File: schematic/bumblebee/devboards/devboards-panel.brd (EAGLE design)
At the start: 60 x 52 mm, 8 parts

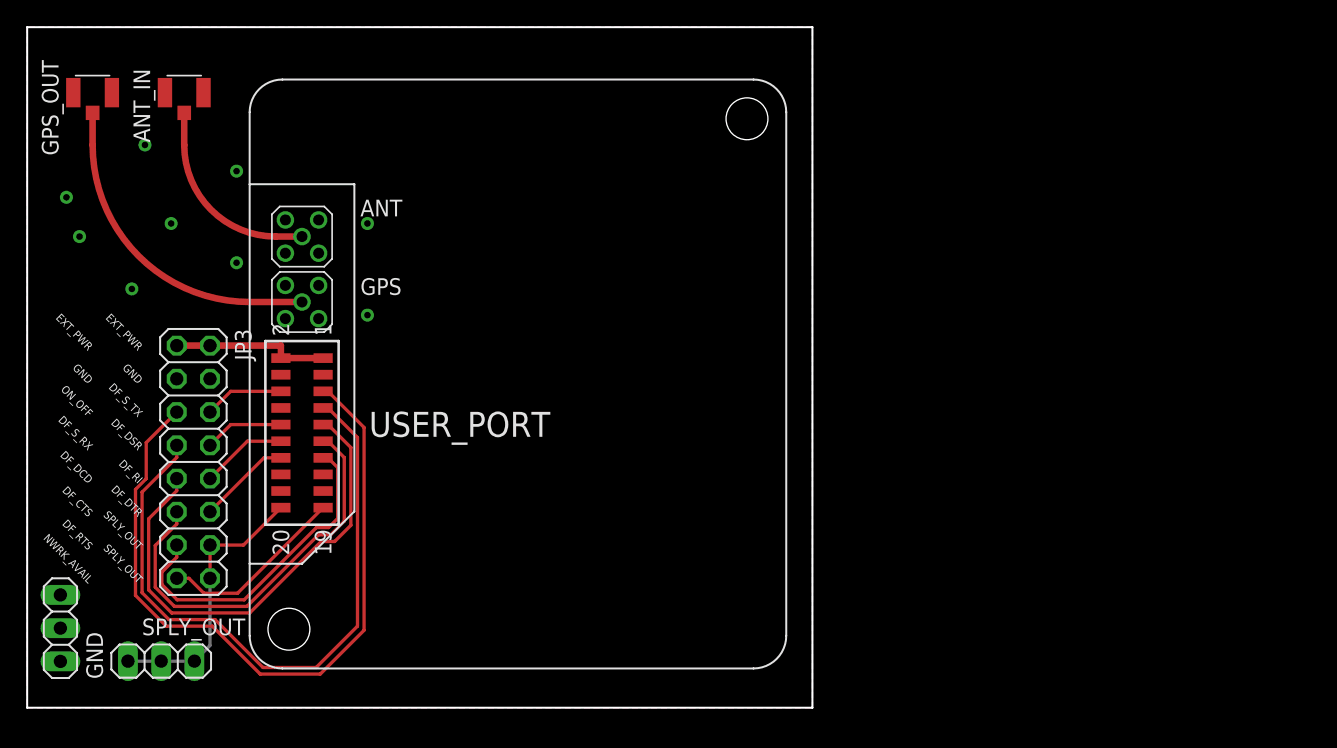
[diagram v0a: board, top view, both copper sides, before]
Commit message: собираем все платы в один шаблон
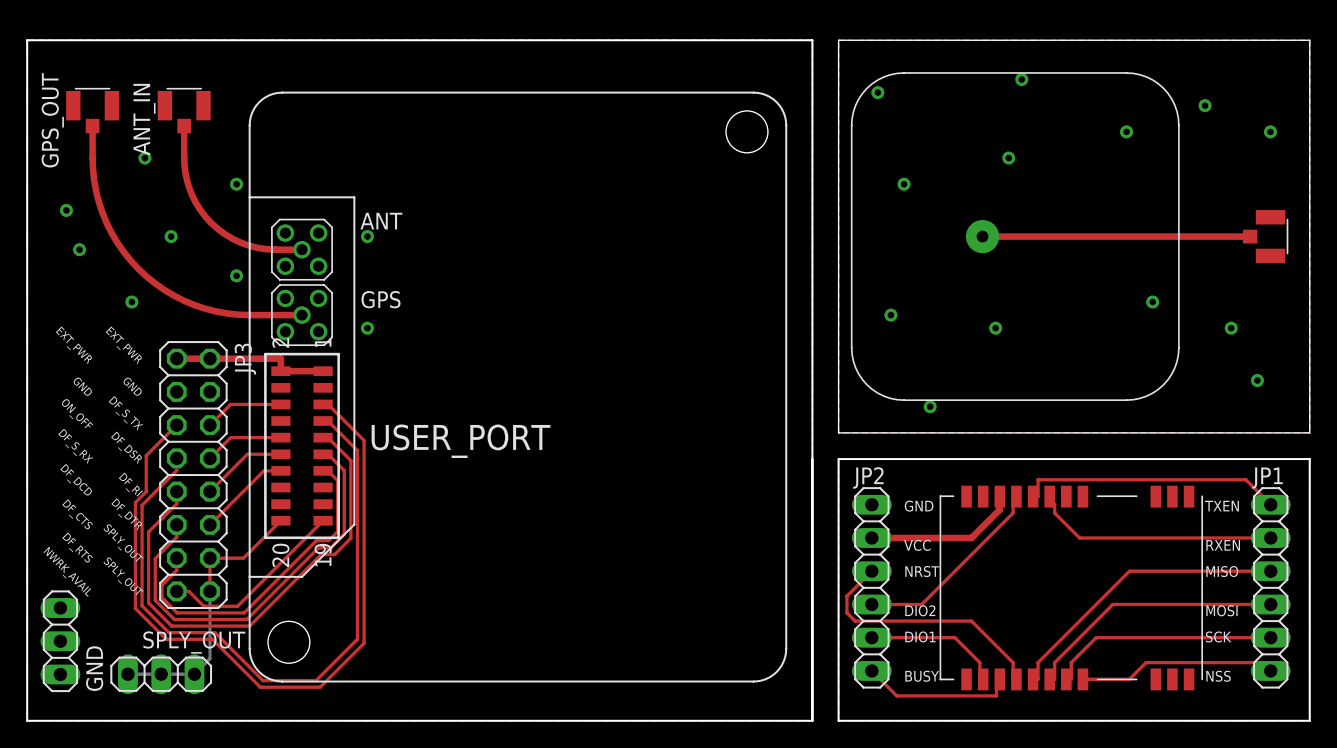
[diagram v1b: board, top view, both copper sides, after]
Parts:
- added J1: U.FL-R-SMT(01), U.FL-R-SMT_01_:HRS_U.FL-R-SMT(01)
- added JP1, JP2: (no value), pinhead:1X06
- added U$1: E22-400M22S, ebyte-radio:E22-400M22S
- added U$2: BY-IRIDIUM-254, iridium-antenna:BY-IRIDIUM-254
- moved ANT 1.00 mm to (21.0, 36.0)
- moved ANT_IN 1.00 mm to (12.0, 47.0)
- moved GND 1.00 mm to (2.54, 6.08)
- moved GPS 1.00 mm to (21.0, 31.0)
- moved GPS_OUT 1.00 mm to (5.00, 47.0)
- moved JP3 1.00 mm to (12.7, 18.8)
- moved USER_PORT 1.00 mm to (21.0, 21.0)
- moved SPLY_OUT 1.00 mm to (10.2, 3.56)
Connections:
- new net BUSY: JP2.6, U$1.P$14
- new net DIO1: JP2.5, U$1.P$13
- new net DIO2: JP2.4, U$1.P$8
- new net GND1: JP2.1, U$1.P$1, U$1.P$10, U$1.P$11, U$1.P$12, U$1.P$2, U$1.P$20, U$1.P$22, U$1.P$3, U$1.P$4, U$1.P$5
- new net MISO: JP1.4, U$1.P$16
- new net MOSI: JP1.3, U$1.P$17
- new net N$1: J1.3, U$2.P$1
- new net NRST: JP2.3, U$1.P$15
- new net NSS: JP1.1, U$1.P$19
- new net RXEN: JP1.5, U$1.P$6
- new net SCK: JP1.2, U$1.P$18
- new net TXEN: JP1.6, U$1.P$7
- new net VCC: JP2.2, U$1.P$9
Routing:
- net MISO: track 0.00 -> 22.3 mm
- net N$1: track 0.00 -> 20.5 mm
- net TXEN: track 0.00 -> 20.2 mm
- net MOSI: track 0.00 -> 20.0 mm
- net NRST: track 0.00 -> 19.8 mm
- net RXEN: track 0.00 -> 18.7 mm
- net SCK: track 0.00 -> 17.7 mm
- net NSS: track 0.00 -> 15.1 mm
- net DIO2: track 0.00 -> 15.0 mm
- net VCC: track 0.00 -> 11.7 mm
- net BUSY: track 0.00 -> 11.6 mm
- net DIO1: track 0.00 -> 10.6 mm
- added copper zone on layer 1, net GND1
- added copper zone on layer 16, net GND1
- added copper zone on layer 1, net GND2
- added copper zone on layer 16, net GND2
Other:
- board size 60 x 52 mm -> 98 x 52 mm
- board text added: "BUSY"
- board text added: "DIO1"
- board text added: "DIO2"
- board text added: "MISO"
- board text added: "MOSI"
- board text added: "NRST"
- board text added: "NSS"
- board text added: "RXEN"
- board text added: "SCK"
- board text added: "TXEN"
- board text added: "VCC"
